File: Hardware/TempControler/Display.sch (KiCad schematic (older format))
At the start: 1 part

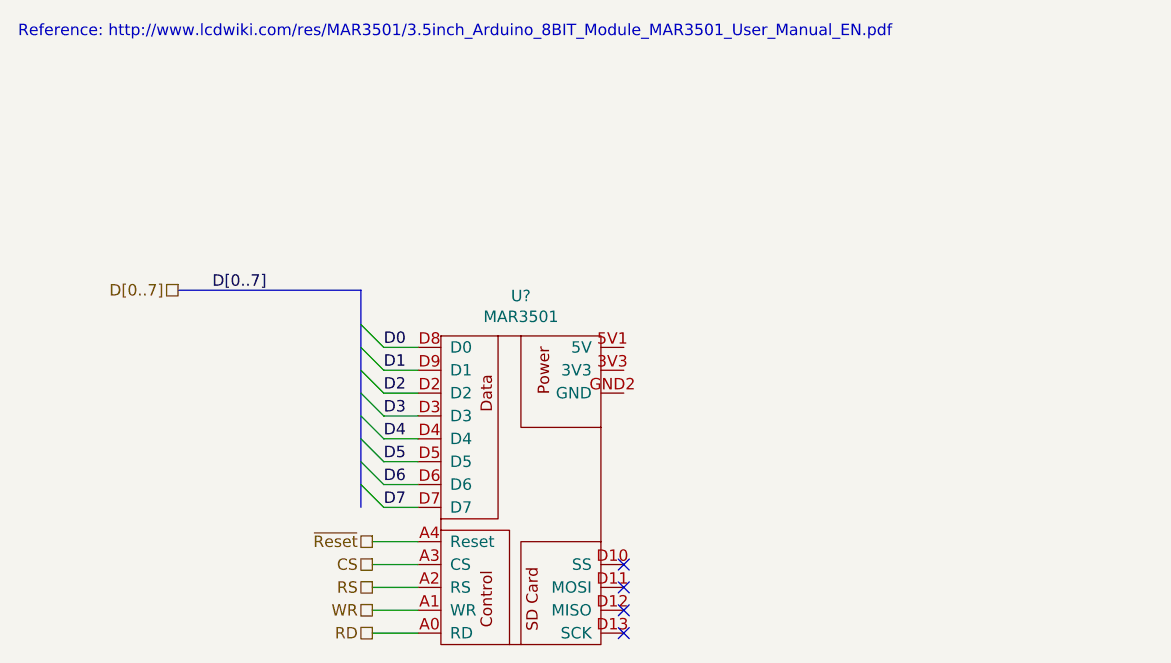
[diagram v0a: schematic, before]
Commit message: Schematic Complete
DRC - Done
Schematic - Done
Values - Done
Part Selection - In Progress
Footprint assignment- In Progress
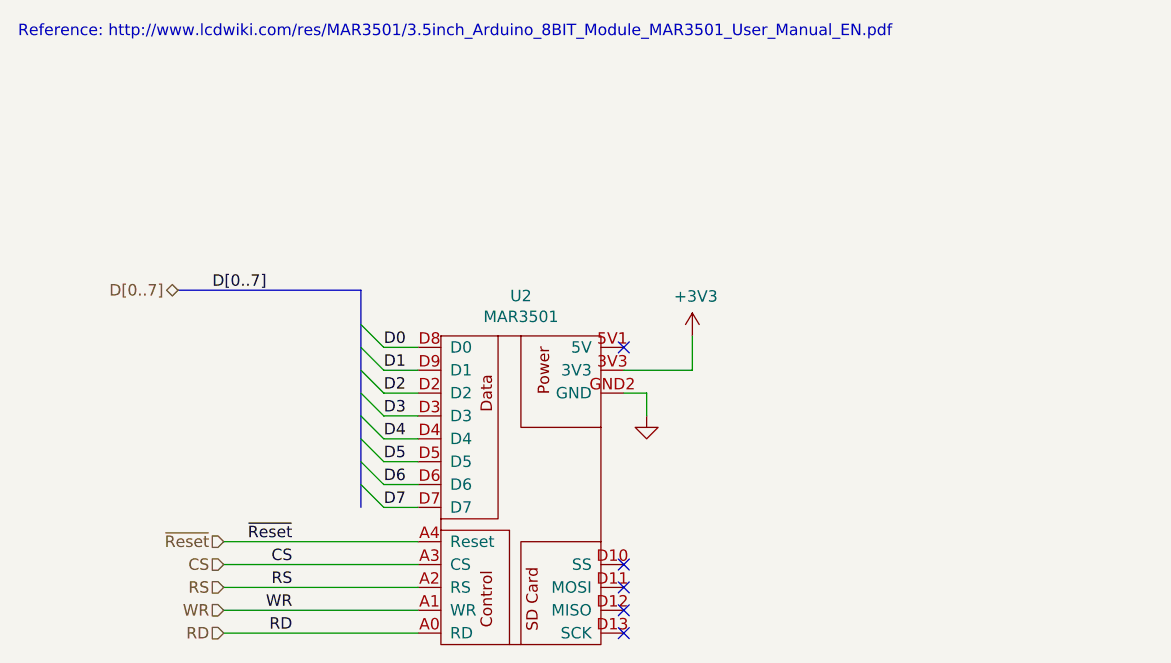
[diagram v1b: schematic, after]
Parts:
- gave numbers to parts that had none: 1
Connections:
- net +3V3: now reaches U2.3V3
- net GND: now reaches U2.GND2 (GND)
- no-connect marks 4 -> 5
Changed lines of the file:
@@
 $Descr USLetter 11000 8500
 encoding utf-8
-Sheet 3 7
+Sheet 3 8
 Title ""
 Date ""
@@
 $EndDescr
 $Comp
-L TFT_LCD_Displays:MAR3501 U?
+L TFT_LCD_Displays:MAR3501 U2
 U 1 1 62D5108A
 P 4700 2850
-F 0 "U?" H 4700 3775 50  0000 C CNN
+F 0 "U2" H 4700 3775 50  0000 C CNN
 F 1 "MAR3501" H 4700 3684 50  0000 C CNN
 F 2 "" H 4700 3250 50  0001 C CNN
@@
 NoConn ~ 5150 3300
 NoConn ~ 5150 3400
-Text HLabel 3200 1900 0    50   UnSpc ~ 0
+Text HLabel 3200 1900 0    50   3State ~ 0
 D[0..7]
-Text HLabel 4050 3000 0    50   UnSpc ~ 0
+Text HLabel 3400 3000 0    50   Input ~ 0
 ~Reset
-Text HLabel 4050 3100 0    50   UnSpc ~ 0
+Text HLabel 3400 3100 0    50   Input ~ 0
 CS
-Text HLabel 4050 3200 0    50   UnSpc ~ 0
+Text HLabel 3400 3200 0    50   Input ~ 0
 RS
-Text HLabel 4050 3300 0    50   UnSpc ~ 0
+Text HLabel 3400 3300 0    50   Input ~ 0
 WR
-Text HLabel 4050 3400 0    50   UnSpc ~ 0
+Text HLabel 3400 3400 0    50   Input ~ 0
 RD
 Entry Wire Line
@@
 Wire Wire Line
 	4250 2850 4100 2850
-Wire Wire Line
-	4250 3000 4050 3000
-Wire Wire Line
-	4250 3100 4050 3100
-Wire Wire Line
-	4250 3200 4050 3200
-Wire Wire Line
-	4250 3300 4050 3300
-Wire Wire Line
-	4250 3400 4050 3400
 Text Label 4100 2150 0    50   ~ 0
 D0
@@
 Text Label 3350 1900 0    50   ~ 0
 D[0..7]
+Text Notes 2500 800  0    50   ~ 0
+Reference: http://www.lcdwiki.com/res/MAR3501/3.5inch_Arduino_8BIT_Module_MAR3501_User_Manual_EN.pdf
+$Comp
+L power:GND #PWR0107
+U 1 1 630030F9
+P 5250 2450
+F 0 "#PWR0107" H 5250 2200 50  0001 C CNN
+F 1 "GND" H 5255 2277 50  0001 C CNN
+F 2 "" H 5250 2450 50  0001 C CNN
+F 3 "" H 5250 2450 50  0001 C CNN
+	1    5250 2450
+	1    0    0    -1
+$EndComp
+Wire Wire Line
+	5250 2450 5250 2350
+Wire Wire Line
+	5250 2350 5150 2350
+$Comp
+L power:+3V3 #PWR0108
+U 1 1 63003925
+P 5450 2100
+F 0 "#PWR0108" H 5450 1950 50  0001 C CNN
+F 1 "+3V3" H 5465 2273 50  0000 C CNN
+F 2 "" H 5450 2100 50  0001 C CNN
+F 3 "" H 5450 2100 50  0001 C CNN
+	1    5450 2100
+	1    0    0    -1
+$EndComp
+Wire Wire Line
+	5450 2100 5450 2250
+Wire Wire Line
+	5450 2250 5150 2250
+Wire Wire Line
+	3400 3000 4250 3000
+Wire Wire Line
+	3400 3100 4250 3100
+Wire Wire Line
+	3400 3200 4250 3200
+Wire Wire Line
+	3400 3300 4250 3300
+Wire Wire Line
+	3400 3400 4250 3400
+Text Label 3700 3000 2    50   ~ 0
+~Reset
+Text Label 3700 3100 2    50   ~ 0
+CS
+Text Label 3700 3200 2    50   ~ 0
+RS
+Text Label 3700 3300 2    50   ~ 0
+WR
+Text Label 3700 3400 2    50   ~ 0
+RD
+NoConn ~ 5150 2150
 Wire Bus Line
 	4000 1900 4000 2850
-Text Notes 2500 800  0    50   ~ 0
-Reference: http://www.lcdwiki.com/res/MAR3501/3.5inch_Arduino_8BIT_Module_MAR3501_User_Manual_EN.pdf
 $EndSCHEMATC

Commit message: All Part Numbers Selected
Next step select all footprints
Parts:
- U2: Mouser (none) -> N/A
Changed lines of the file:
@@
 F 3 "https://www.waveshare.com/w/upload/7/78/ILI9486_Datasheet.pdf" H 4700 3250 50  0001 C CNN
 F 4 "http://www.lcdwiki.com/res/MAR3501/3.5inch_Arduino_8BIT_Module_MAR3501_User_Manual_EN.pdf" H 5050 3800 50  0001 C CNN "User Manual"
+F 5 "N/A" H 4700 2850 50  0001 C CNN "Mouser"
 	1    4700 2850
 	1    0    0    -1

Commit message: Footprints selected
On to board design
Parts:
- U2: footprint (none) -> Shields:Shield_MEGA-LCD
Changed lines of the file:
@@
 U 1 1 62D5108A
 P 4700 2850
+AR Path="/62D5108A" Ref="U2"  Part="1"
+AR Path="/62D4790F/62D5108A" Ref="U2"  Part="1"
 F 0 "U2" H 4700 3775 50  0000 C CNN
 F 1 "MAR3501" H 4700 3684 50  0000 C CNN
-F 2 "" H 4700 3250 50  0001 C CNN
+F 2 "Shields:Shield_MEGA-LCD" H 4700 3250 50  0001 C CNN
 F 3 "https://www.waveshare.com/w/upload/7/78/ILI9486_Datasheet.pdf" H 4700 3250 50  0001 C CNN
 F 4 "http://www.lcdwiki.com/res/MAR3501/3.5inch_Arduino_8BIT_Module_MAR3501_User_Manual_EN.pdf" H 5050 3800 50  0001 C CNN "User Manual"
